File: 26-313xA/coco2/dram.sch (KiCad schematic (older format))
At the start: 7 parts, among them CN3 Conn_01x12_Female, CN4 Conn_01x12_Female, IC10 TMS4416, IC11 TMS4416

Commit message: -Corrected some part numbers in the BOM -Updated paret numbers for some parts in the schematic.
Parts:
- C5, C6: Manufacturer part# FG28C0G1H103JNT06 -> RDER71H104K0K1H03B; Vendor part# 445-173474-1-ND -> 490-8814-ND
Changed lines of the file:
@@
 F 1 ".1uF" H 3850 6850 50  0000 C CNN
 F 2 "Capacitor_THT:C_Disc_D4.7mm_W2.5mm_P5.00mm" H 3650 6800 50  0001 C CNN
-F 3 " https://product.tdk.com/info/en/catalog/datasheets/leadmlcc_halogenfree_fg_en.pdf?ref_disty=digikey" H 3650 6800 50  0001 C CNN
+F 3 " https://search.murata.co.jp/Ceramy/image/img/A01X/G101/ENG/RDE_X7R_250V-1kV_E.pdf" H 3650 6800 50  0001 C CNN
 F 4 "digikey" V 3650 6800 50  0001 C CNN "Vendor"
-F 5 "445-173474-1-ND" V 3650 6800 50  0001 C CNN "Vendor part#"
-F 6 "FG28C0G1H103JNT06" H 3650 6800 50  0001 C CNN "Manufacturer part#"
+F 5 "490-8814-ND" V 3650 6800 50  0001 C CNN "Vendor part#"
+F 6 "RDER71H104K0K1H03B" H 3650 6800 50  0001 C CNN "Manufacturer part#"
 	1    3650 6800
 	-1   0    0    1
@@
 F 1 ".1uF" H 4250 6850 50  0000 C CNN
 F 2 "Capacitor_THT:C_Disc_D4.7mm_W2.5mm_P5.00mm" H 4050 6800 50  0001 C CNN
-F 3 " https://product.tdk.com/info/en/catalog/datasheets/leadmlcc_halogenfree_fg_en.pdf?ref_disty=digikey" H 4050 6800 50  0001 C CNN
+F 3 " https://search.murata.co.jp/Ceramy/image/img/A01X/G101/ENG/RDE_X7R_250V-1kV_E.pdf" H 4050 6800 50  0001 C CNN
 F 4 "digikey" V 4050 6800 50  0001 C CNN "Vendor"
-F 5 "445-173474-1-ND" V 4050 6800 50  0001 C CNN "Vendor part#"
-F 6 "FG28C0G1H103JNT06" H 4050 6800 50  0001 C CNN "Manufacturer part#"
+F 5 "490-8814-ND" V 4050 6800 50  0001 C CNN "Vendor part#"
+F 6 "RDER71H104K0K1H03B" H 4050 6800 50  0001 C CNN "Manufacturer part#"
 	1    4050 6800
 	-1   0    0    1

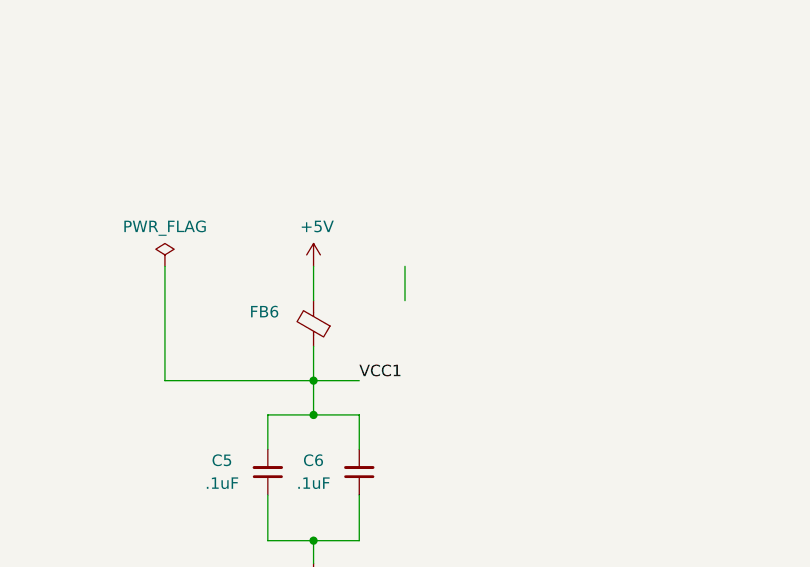
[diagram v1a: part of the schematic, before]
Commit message: -moved power switch 4mm into the board. -moved reset switch 1mm towards the DIN connectors. -moved channel select switch .5mm into the DIN connectors. -shortened length of board from cart to power connector 1mm. -updated image,layout,schematic and BOM's
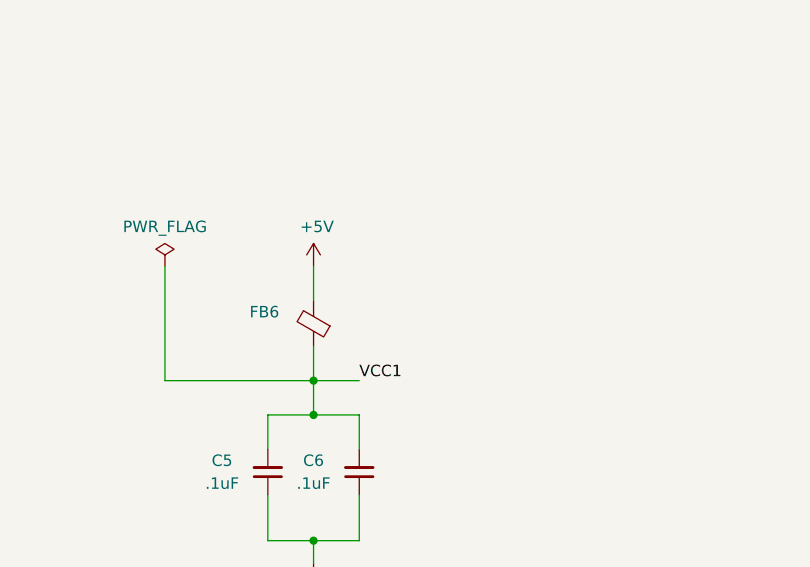
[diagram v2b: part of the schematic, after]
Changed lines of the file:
@@
 $EndComp
-Wire Wire Line
-	4250 5900 4250 6050
 Wire Wire Line
 	3850 6400 3200 6400
